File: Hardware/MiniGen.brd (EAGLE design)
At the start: 17.8 x 33 mm, 32 parts, among them U1 16MHz, U2 3.3V, U3 AD9837

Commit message: Added version info.
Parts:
- removed U$3: CREATIVE_COMMONS, SparkFun-Aesthetics:CREATIVE_COMMONS
- added FRAME1: FRAME-LETTER, SparkFun-Aesthetics:CREATIVE_COMMONS
- moved C10 3.81 mm to (11.4, 12.7)
- moved C4 3.81 mm to (14.0, 12.7)
- moved JP4 3.81 mm to (9.53, 26.9)
- moved LED1 3.81 mm to (8.89, 24.1)
- moved R1 3.81 mm to (8.89, 25.4)
- moved R7 3.81 mm to (12.7, 12.7)
- moved R8 3.81 mm to (6.99, 12.7)
- moved SJ1 3.81 mm to (8.89, 29.6)
- moved U2 3.81 mm to (8.89, 29.2)
- moved C13 3.81 mm to (6.99, 15.7)
- moved C9 3.81 mm to (3.43, 14.0)
- moved J1 3.81 mm to (12.7, 2.16)
- moved R10 3.81 mm to (4.83, 14.0)
- moved U$2 3.81 mm to (7.75, 5.71)
- moved JP2 3.81 mm to (5.08, 1.27)
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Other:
- board text added: "v03"
- board text removed: "v0.1"

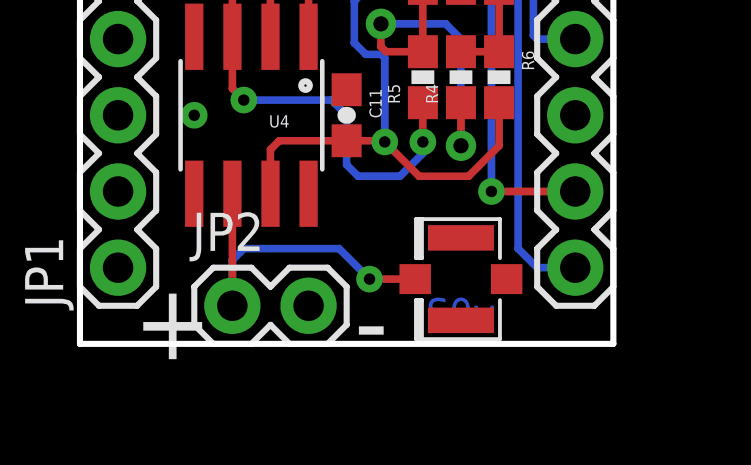
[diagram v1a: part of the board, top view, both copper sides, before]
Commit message: Advance design to v10 for release.
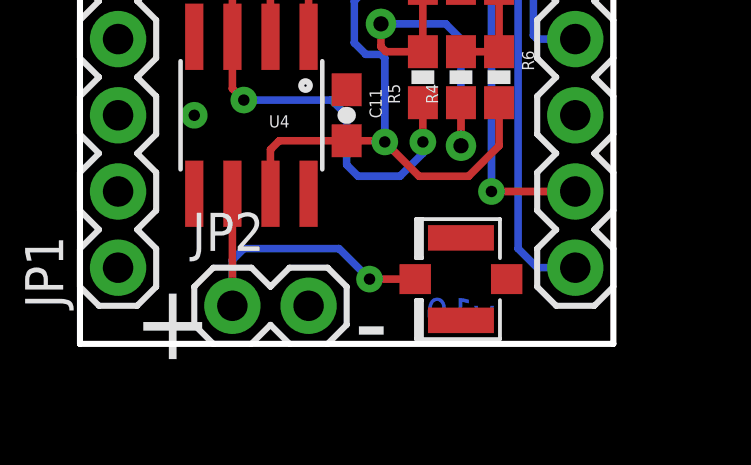
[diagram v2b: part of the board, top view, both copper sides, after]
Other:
- board text added: "v10"
- board text removed: "v03"
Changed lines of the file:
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@@
 <text x="15.113" y="4.572" size="1.016" layer="22" font="vector" ratio="15" rot="MR0">SDATA</text>
 <text x="2.413" y="20.701" size="0.8128" layer="22" font="vector" ratio="15" rot="MR180">FSYNC</text>
-<text x="13.843" y="0.508" size="1.016" layer="16" font="vector" ratio="15" rot="MR0">v03</text>
+<text x="13.843" y="0.508" size="1.016" layer="16" font="vector" ratio="15" rot="MR0">v10</text>
 <text x="21.59" y="-13.97" size="1.778" layer="51" font="vector" ratio="15">Pete Dokter and Anne Mahaffey</text>
 </plain>

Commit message: Fix labeling on schematic
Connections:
- net N$1 renamed OUT
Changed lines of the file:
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@@
 <text x="15.113" y="9.652" size="1.016" layer="22" font="vector" ratio="15" rot="MR0">SCLK</text>
 <text x="15.113" y="4.572" size="1.016" layer="22" font="vector" ratio="15" rot="MR0">SDATA</text>
-<text x="2.413" y="20.701" size="0.8128" layer="22" font="vector" ratio="15" rot="MR180">FSYNC</text>
+<text x="11.303" y="2.921" size="0.8128" layer="22" font="vector" ratio="15" rot="MR180">FSYNC</text>
 <text x="13.843" y="0.508" size="1.016" layer="16" font="vector" ratio="15" rot="MR0">v10</text>
 <text x="21.59" y="-13.97" size="1.778" layer="51" font="vector" ratio="15">Pete Dokter and Anne Mahaffey</text>
@@
 <wire x1="7.62" y1="11.684" x2="7.835" y2="11.899" width="0.254" layer="1"/>
 </signal>
-<signal name="N$1">
+<signal name="OUT">
 <contactref element="JP2" pad="1"/>
 <contactref element="J1" pad="P$3"/>
